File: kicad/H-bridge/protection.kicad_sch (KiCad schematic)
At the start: 29 parts, among them U4 LT1011, U5 LM340MPX-5.0/NOPB, U6 74LVC1G373, U8 74AC14DR

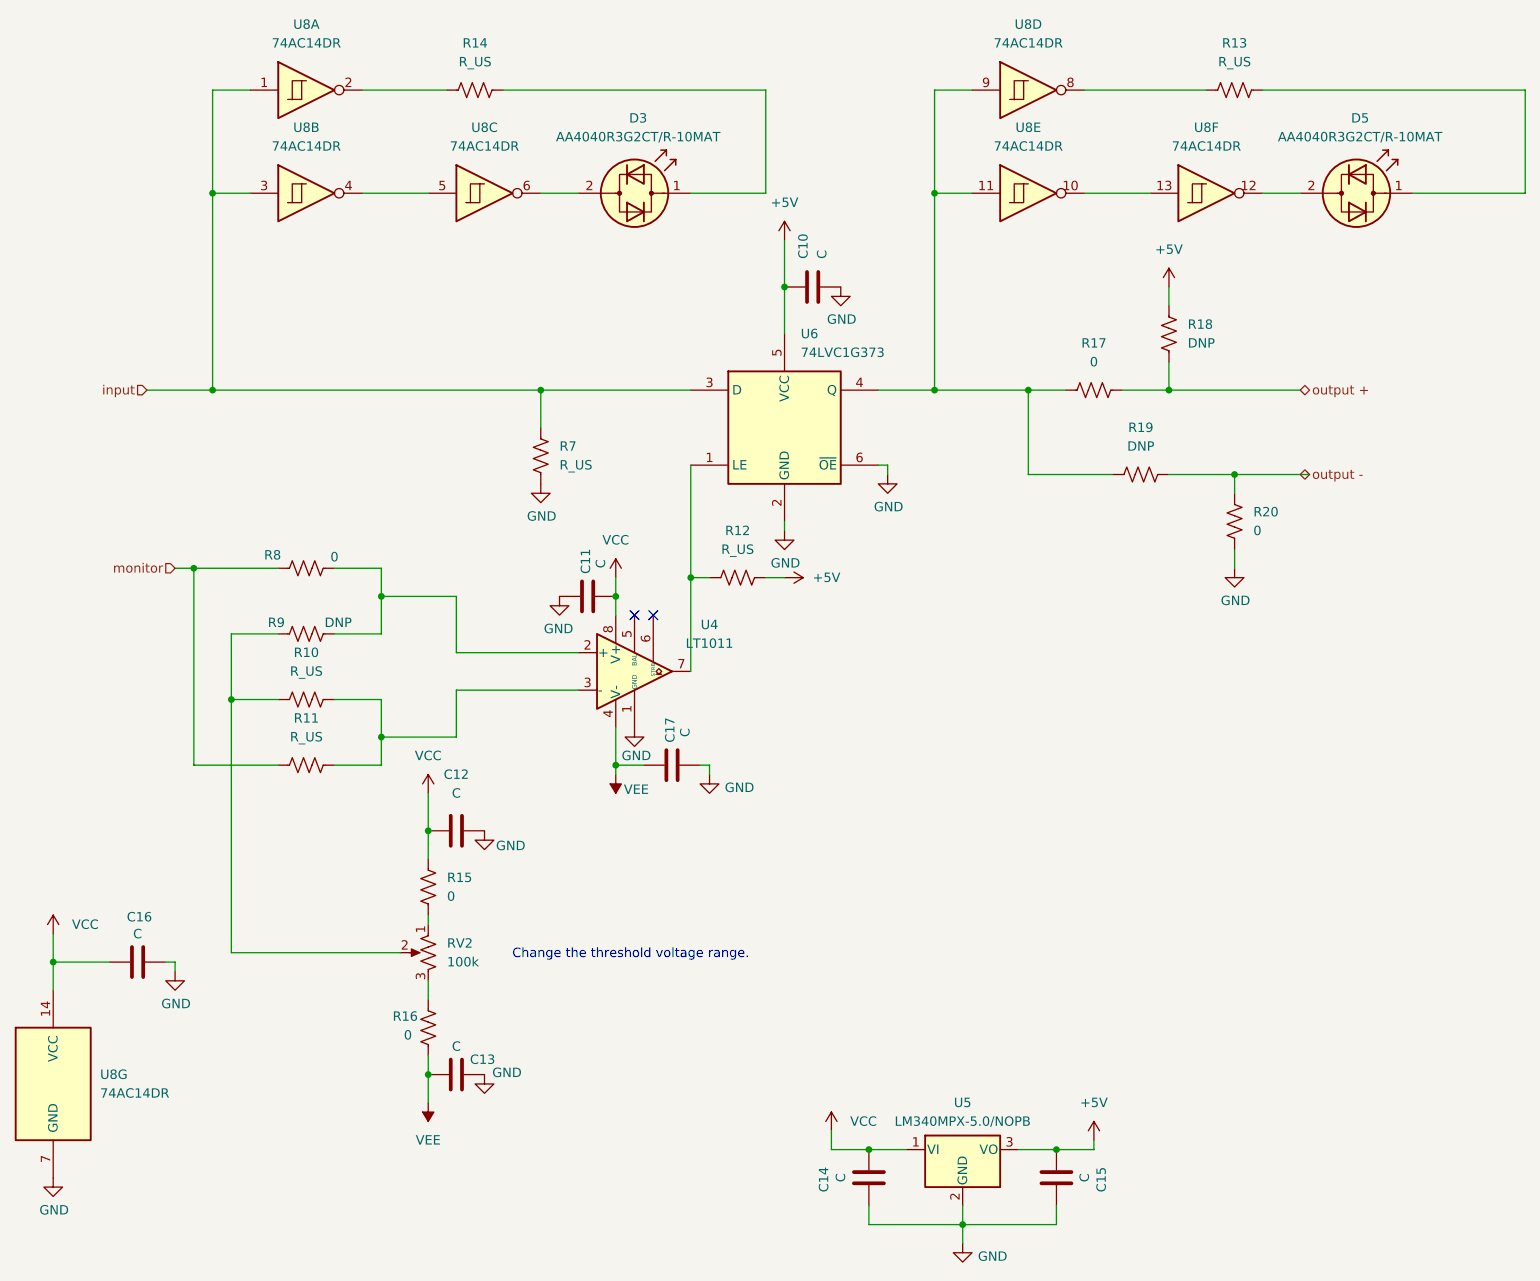
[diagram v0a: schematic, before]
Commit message: Added C18, logo and other footprints
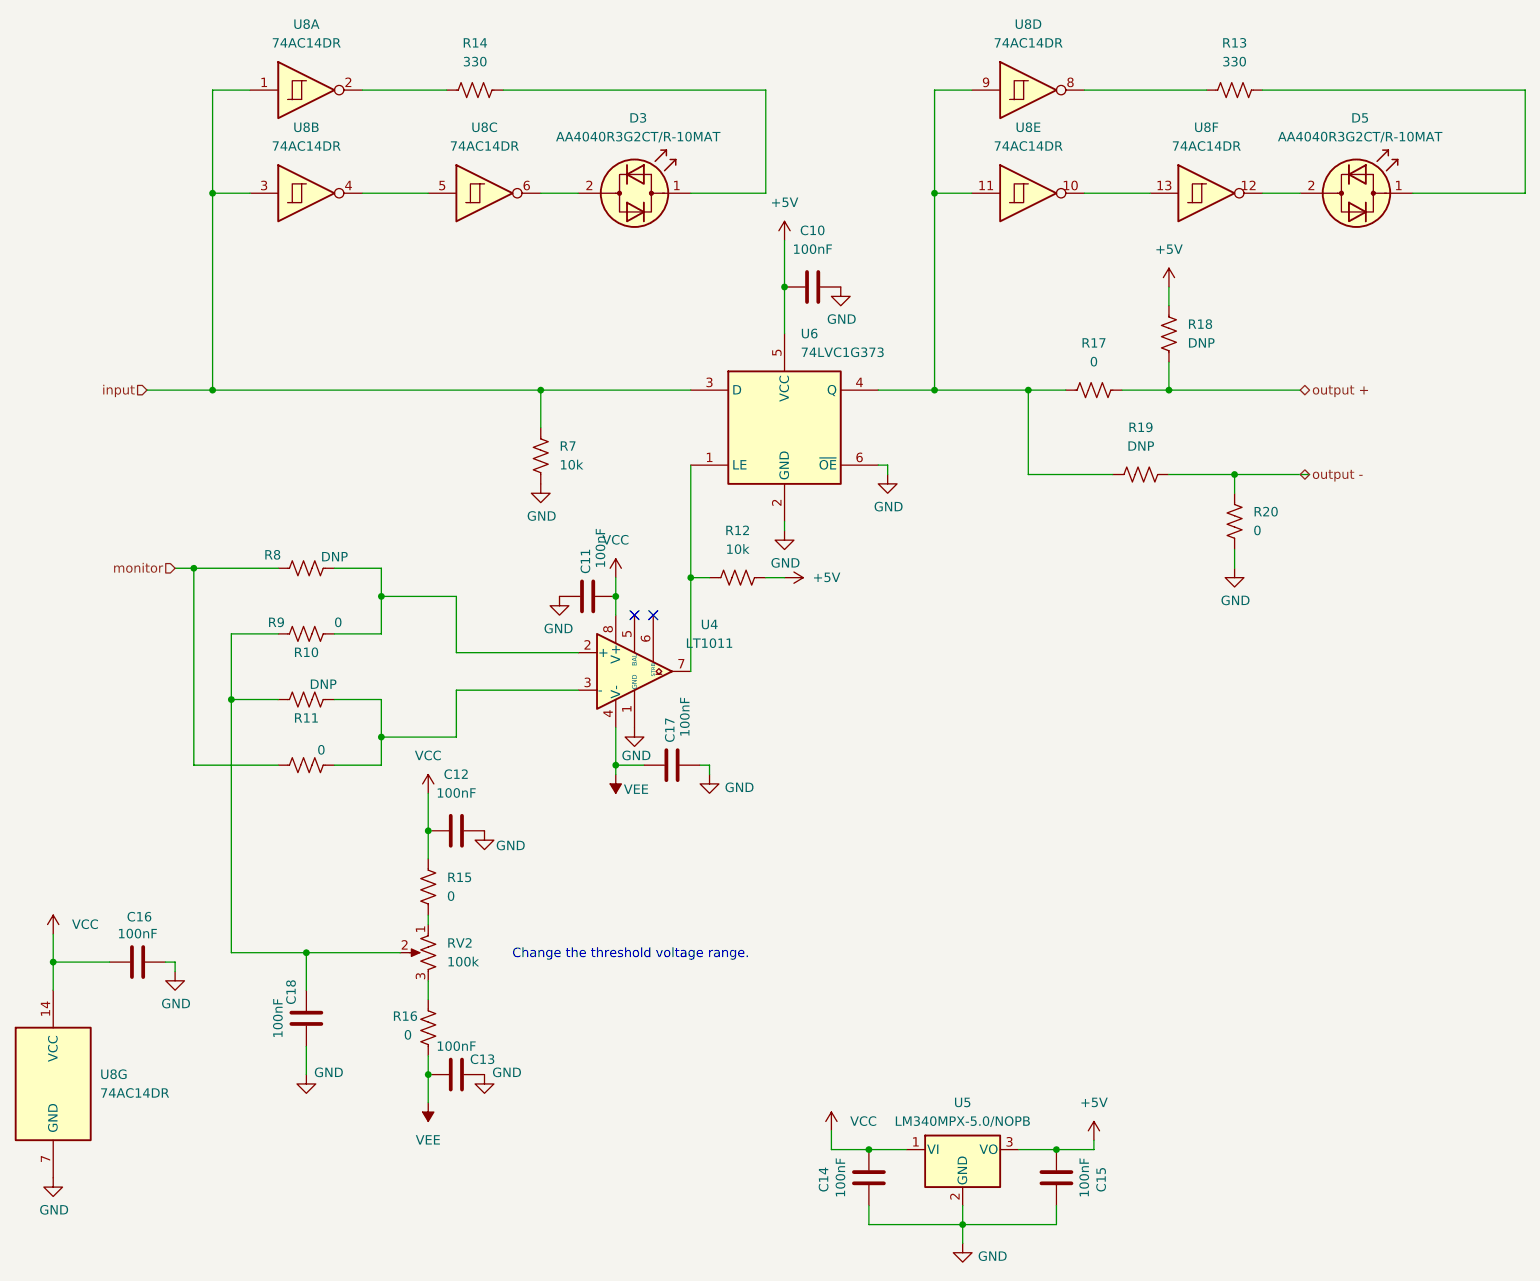
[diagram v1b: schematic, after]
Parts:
- added C18: 100nF, Capacitor_SMD:C_0805_2012Metric, symbol Device:C
- C10, C11, C12, C13, C14, C15, C16, C17: value C -> 100nF; DIGIKEY (none) -> 311-1140-1-ND; PARTNO (none) -> CC0805KRX7R9BB104
- R10: value R_US -> DNP
- R11: value R_US -> 0; DIGIKEY (none) -> A106066CT-ND; PARTNO (none) -> CRG0805ZR
- R12, R7: value R_US -> 10k; DIGIKEY (none) -> A129761CT-ND; PARTNO (none) -> CRGCQ0805F10K
- R13, R14: value R_US -> 330; DIGIKEY (none) -> A129743CT-ND; PARTNO (none) -> CRGCQ0805F330R
- R15, R16, R17, R20: DIGIKEY (none) -> A106066CT-ND; PARTNO (none) -> CRG0805ZR
- R8: value 0 -> DNP
- R9: value DNP -> 0; DIGIKEY (none) -> A106066CT-ND; PARTNO (none) -> CRG0805ZR
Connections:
- net GND: now also C18.1
- net at R10.1, R9.1, RV2.2: now also C18.2
